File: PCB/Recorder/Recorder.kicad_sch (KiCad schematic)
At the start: 47 parts, among them J1 Battery, J2 Reset, J3 TC2030-USB-NL-DS, J4 TF_PUSH, J5 USB-C-Socket-H, Q2 CJ2301, SW1 SW_Push, U1 R, U2 L, U3 TP4054, U4 ME6211C33M5G-N, U6 ESP32-S3-MINI-1

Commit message: Started new Intercom
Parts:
- U6: value ESP32-S3-MINI-1 -> ESP32-S3-MINI-1-N4R2
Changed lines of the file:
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@@
 			)
 		)
-		(property "Value" "ESP32-S3-MINI-1"
+		(property "Value" "ESP32-S3-MINI-1-N4R2"
 			(at 50.8 45.5696 0)
 			(effects

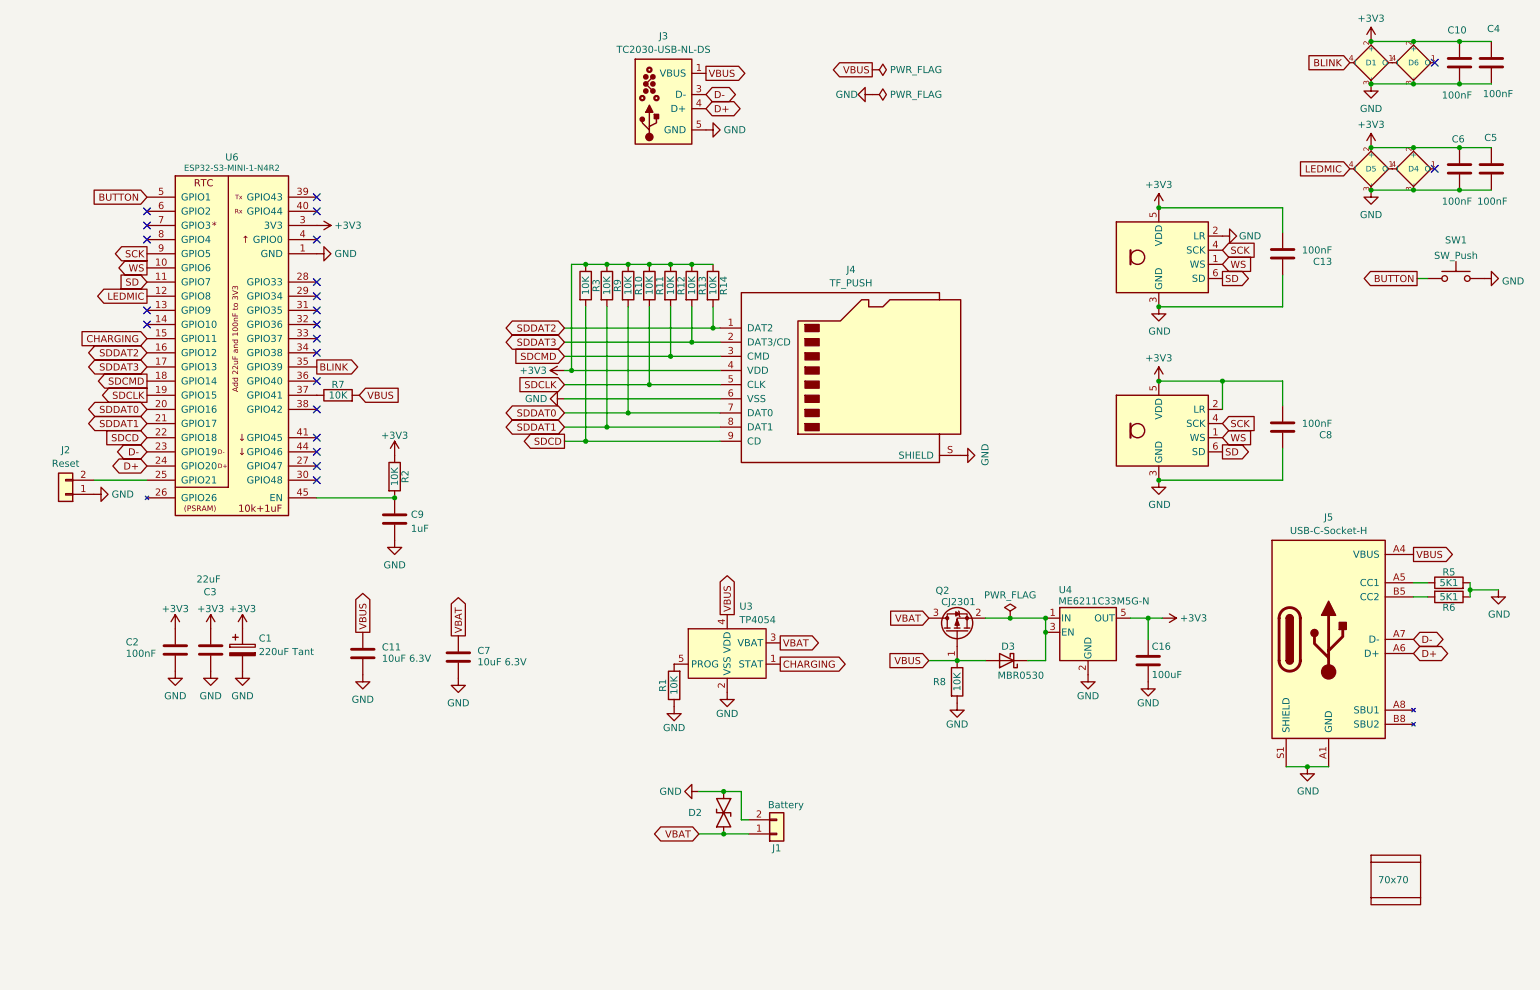
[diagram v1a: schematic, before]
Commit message: Power control for LEDs
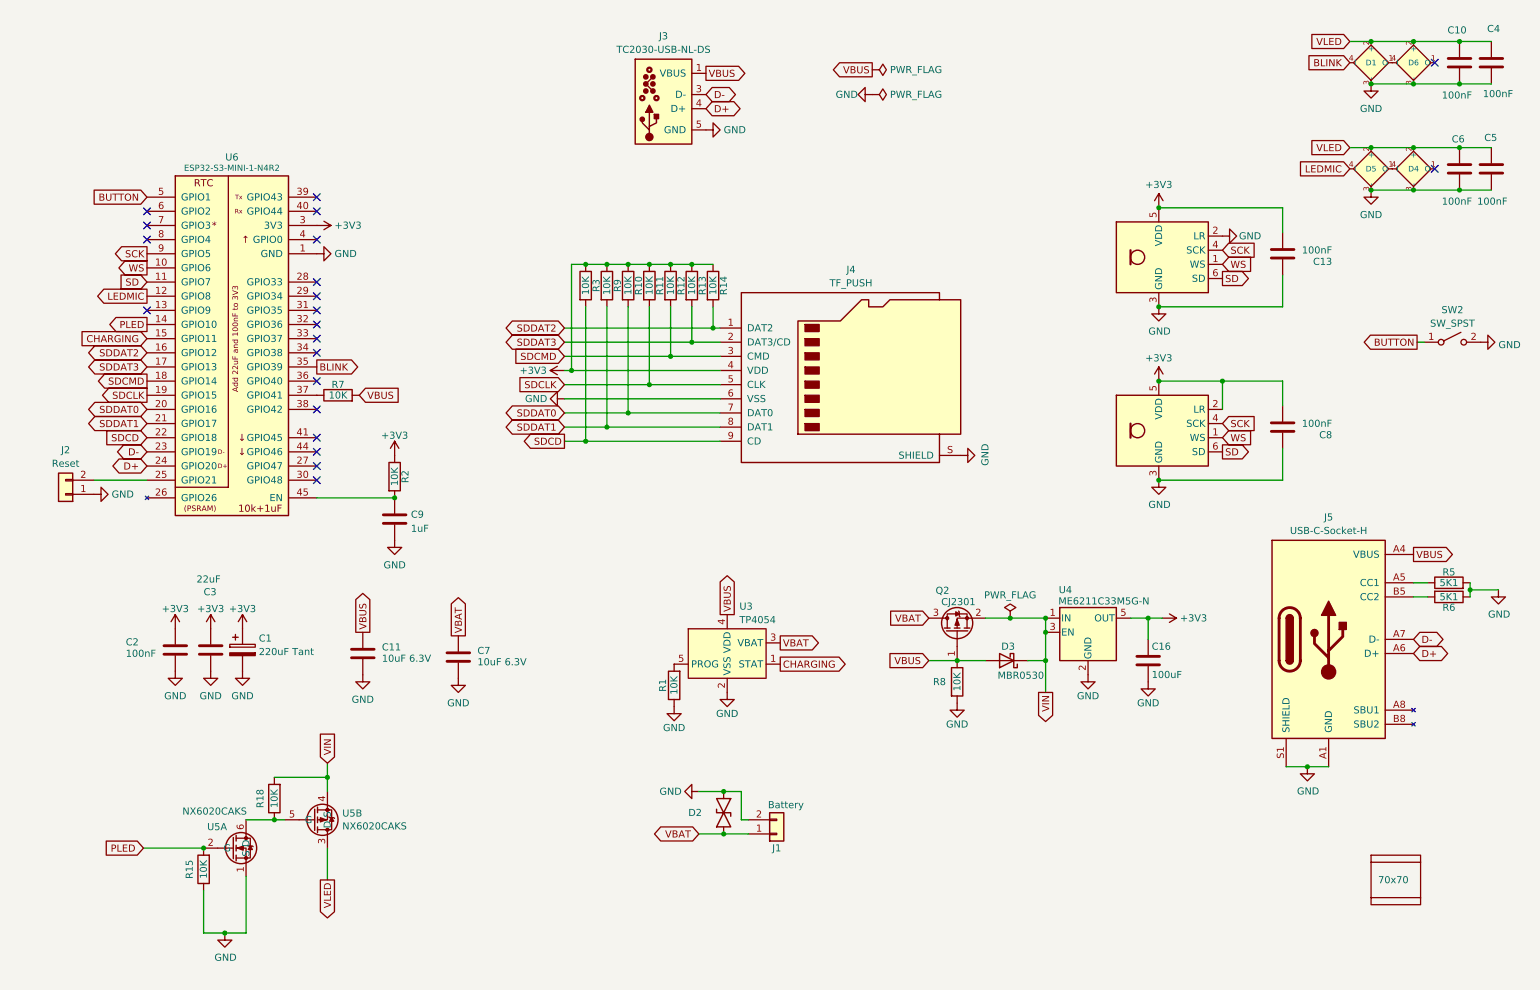
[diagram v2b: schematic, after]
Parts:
- removed SW1: SW_Push, RevK:TS-1092S-B3D2-G, symbol Switch:SW_Push
- added R15, R18: 10K, RevK:R_0402, symbol Device:R
- added SW2: SW_SPST, Button_Switch_SMD:SW_Push_1TS009xxxx-xxxx-xxxx_6x6x5mm, symbol Switch:SW_SPST
- added U5: NX6020CAKS, RevK:SOT-363_SC-70-6, symbol RevK:NX6020CAKS
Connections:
- net +3V3: no longer C10.1, C4.1, C5.1, C6.1, D1.2 (+), D4.2 (+), D5.2 (+), D6.2 (+)
- net BUTTON: now also SW2.1 (A)
- net GND: now also R15.1, SW2.2 (B), U5.1 (S)
- net VIN: now reaches D3.1 (K), Q2.2 (S), U4.1 (IN), U4.3 (EN)
- net VIN: now also R18.2, U5.4 (S)
- net PLED: now reaches U6.14 (GPIO10)
- net PLED: now also R15.2, U5.2 (G)
- new net: R18.1, U5.5 (G), U5.6 (D)
- new net VLED: C10.1, C4.1, C5.1, C6.1, D1.2 (+), D4.2 (+), D5.2 (+), D6.2 (+), U5.3 (D)
- no-connect marks 22 -> 21

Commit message: Clean up
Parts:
- U4: footprint RevK:SOT-23-5 -> RevK:SOT-23-5-90
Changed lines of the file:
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@@
 			)
 		)
-		(property "Footprint" "RevK:SOT-23-5"
+		(property "Footprint" "RevK:SOT-23-5-90"
 			(at 204.47 120.65 0)
 			(effects

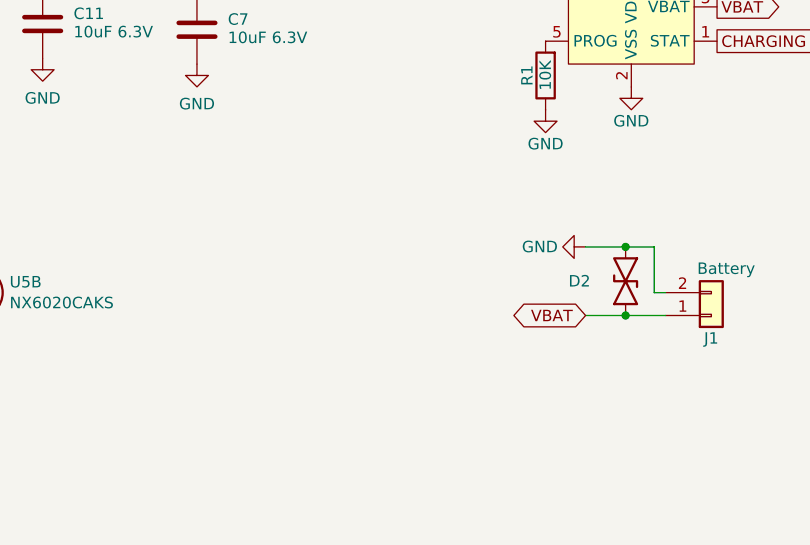
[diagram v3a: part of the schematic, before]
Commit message: New battery case
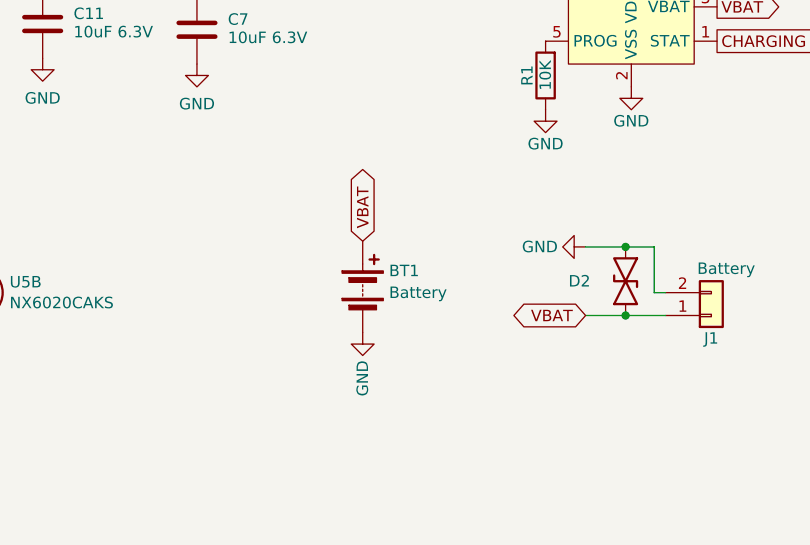
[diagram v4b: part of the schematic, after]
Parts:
- added BT1: Battery, RevK:LiPo1, symbol Device:Battery
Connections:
- net GND: now also BT1.2 (-)
- net VBAT: now also BT1.1 (+)
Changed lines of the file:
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@@
+		)
+	)
+	(global_label "VBAT"
+		(shape bidirectional)
+		(at 109.855 156.845 90)
+		(fields_autoplaced yes)
+		(effects
+			(font
+				(size 1.27 1.27)
+			)
+			(justify left)
+		)
+		(property "Intersheetrefs" "${INTERSHEET_REFS}"
+			(at 109.855 149.1467 90)
+			(effects
+				(font
+					(size 1.27 1.27)
+				)
+				(justify left)
+				(hide yes)
+			)
 		)
 	)
@@
 	)
 	(symbol
+		(lib_id "power:GND")
+		(at 109.855 167.005 0)
+		(unit 1)
+		(exclude_from_sim no)
+		(in_bom yes)
+		(on_board yes)
+		(dnp no)
+		(property "Reference" "#PWR030"
+			(at 109.855 173.355 0)
+			(effects
+				(font
+					(size 1.27 1.27)
+				)
+				(hide yes)
+			)
+		)
+		(property "Value" "GND"
+			(at 109.855 172.085 90)
+			(effects
+				(font
+					(size 1.27 1.27)
+				)
+			)
+		)
+		(property "Footprint" ""
+			(at 109.855 167.005 0)
+			(effects
+				(font
+					(size 1.27 1.27)
+				)
+				(hide yes)
+			)
+		)
+		(property "Datasheet" ""
+			(at 109.855 167.005 0)
+			(effects
+				(font
+					(size 1.27 1.27)
+				)
+				(hide yes)
+			)
+		)
+		(property "Description" "Power symbol creates a global label with name \"GND\" , ground"
+			(at 109.855 167.005 0)
+			(effects
+				(font
+					(size 1.27 1.27)
+				)
+				(hide yes)
+			)
+		)
+		(pin "1"
+		)
+		(instances
+			(project "Recorder"
+				(path "/46c350bb-7de4-4e81-aafd-4af55e37aab0"
+					(reference "#PWR030")
+					(unit 1)
+				)
+			)
+		)
+	)
+	(symbol
 		(lib_id "Device:C")
 		(at 74.295 132.715 0)
@@
 					(unit 1)
 				)
+			)
+		)
+	)
+	(symbol
+		(lib_id "Device:Battery")
+		(at 109.855 161.925 0)
+		(unit 1)
+		(exclude_from_sim no)
+		(in_bom no)
+		(on_board yes)
+		(dnp no)
+		(fields_autoplaced yes)
+		(property "Reference" "BT1"
+			(at 112.776 160.1413 0)
+			(effects
+				(font
+					(size 1.27 1.27)
+				)
+				(justify left)
+			)
+		)
+		(property "Value" "Battery"
+			(at 112.776 162.5656 0)
+			(effects
+				(font
+					(size 1.27 1.27)
+				)
+				(justify left)
+			)
+		)
+		(property "Footprint" "RevK:LiPo1"
+			(at 109.855 160.401 90)
+			(effects
+				(font
+					(size 1.27 1.27)
+				)
+				(hide yes)
+			)
+		)
+		(property "Datasheet" "~"
+			(at 109.855 160.401 90)
+			(effects
+				(font
+					(size 1.27 1.27)
+				)
+				(hide yes)
+			)
+		)
+		(property "Description" "Multiple-cell battery"
+			(at 109.855 161.925 0)
+			(effects
+				(font
+					(size 1.27 1.27)
+				)
+				(hide yes)
+			)
+		)
+		(pin "1"
+		)
+		(pin "2"
+		)
+		(instances
+			(project ""
+				(path "/46c350bb-7de4-4e81-aafd-4af55e37aab0"
+					(reference "BT1")
+					(unit 1)
+				)

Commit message: Library update
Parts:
- removed C7: 10uF 6.3V, RevK:C_0402, symbol Device:C
- removed J1: Battery, RevK:1.25T-2PWT (Molex 532610271), symbol Connector_Generic:Conn_01x02
- removed R18: 10K, RevK:R_0402, symbol Device:R
- removed SW2: SW_SPST, Button_Switch_SMD:SW_Push_1TS009xxxx-xxxx-xxxx_6x6x5mm, symbol Switch:SW_SPST
- removed U5: NX6020CAKS, RevK:SOT-363_SC-70-6, symbol RevK:NX6020CAKS
- added C1, C3: 22uF, RevK:C_0603, symbol Device:C
- added D1: D, RevK:D_0402, symbol Device:D
- added D10, D6, D8: XL-1010RGBC-WS2812B, RevK:SMD1010, symbol RevK:WS2812B-1mm
- added J6: Battery, RevK:1.25T-2PWT (Molex 532610271), symbol Connector_Generic:Conn_01x02
- added R14, R16: 100K 1%, RevK:R_0201, symbol Device:R
- added SW1: SW_Push_DPDT, RevK:SW_Push_DPDT, symbol RevK:SW_Push_DPDT
- added TP1, TP2: TestPoint, RevK:PAD-2mm, symbol Connector:TestPoint
- added U2: TPS22916CNYFPR, RevK:WCSP-4-0.78x0.78, symbol RevK:TPS22916
- C10: renamed from C13; footprint RevK:C_0402 -> RevK:C_0201
- C11: renamed from C8; footprint RevK:C_0402 -> RevK:C_0201
- C12: renamed from C10; footprint RevK:C_0402 -> RevK:C_0201
- C13: renamed from C6; footprint RevK:C_0402 -> RevK:C_0201
- C14: renamed from C4; footprint RevK:C_0402 -> RevK:C_0201
- C15: renamed from C5; footprint RevK:C_0402 -> RevK:C_0201
- C2: renamed from C9; footprint RevK:C_0402 -> RevK:C_0201
- C4: renamed from C2; footprint RevK:C_0402 -> RevK:C_0201
- R1: renamed from R7; footprint RevK:R_0402 -> RevK:R_0201; MPN (none) -> C106225
- R10: renamed from R14; footprint RevK:R_0402 -> RevK:R_0201; MPN (none) -> C106225
- R11: renamed from R8; footprint RevK:R_0402 -> RevK:R_0201; MPN (none) -> C106225
- R12: renamed from R5; footprint RevK:R_0402 -> RevK:R_0201; MPN (none) -> C274341
- R13: renamed from R6; footprint RevK:R_0402 -> RevK:R_0201; MPN (none) -> C274341
- R15: value 10K -> 100K 1%; footprint RevK:R_0402 -> RevK:R_0201; MPN (none) -> C717003
- R2, R3: footprint RevK:R_0402 -> RevK:R_0201; MPN (none) -> C106225
- R4: renamed from R9; footprint RevK:R_0402 -> RevK:R_0201; MPN (none) -> C106225
- R5: renamed from R10; footprint RevK:R_0402 -> RevK:R_0201; MPN (none) -> C106225
- R6: renamed from R11; footprint RevK:R_0402 -> RevK:R_0201; MPN (none) -> C106225
- R7: renamed from R12; footprint RevK:R_0402 -> RevK:R_0201; MPN (none) -> C106225
- R8: renamed from R1; value 10K -> 5K1; footprint RevK:R_0402 -> RevK:R_0201; MPN (none) -> C274341
- R9: renamed from R13; footprint RevK:R_0402 -> RevK:R_0201; MPN (none) -> C106225
- U4: Rotation Offset (none) -> 90
- U5: renamed from U2; value L -> ICS-43434
- U6: renamed from U1; value R -> ICS-43434
- renumbered C3 to C5, C1 to C6, C11 to C7, C16 to C9, D1 to D4, D6 to D5, D5 to D7, D4 to D9, J2 to J1, Q2 to Q1, U6 to U1
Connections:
- net BUTTON is gone; now on net CHARGING: U1.5 (GPIO1)
- net VLED is gone; now on net +3V3: C12.1, C13.1, C14.1, C15.1, D4.2 (+), D5.2 (+), D7.2 (+), D9.2 (+)
- net +3V3: now also D10.2 (+), D6.2 (+), D8.2 (+)
- net BLINK: now also U1.8 (GPIO4); no longer U1.35 (GPIO39)
- net CHARGING: no longer U1.15 (GPIO11)
- net D+: now also TP2.1
- net D-: now also TP1.1
- net GND: now also C1.2, C3.2, D10.3 (-), D6.3 (-), D8.3 (-), J6.2 (Pin_2), R16.2, SW1.5 (B), U2.B1 (GND); no longer R15.1
- net LEDMIC: now also U1.13 (GPIO9); no longer U1.12 (GPIO8)
- net at D5.1 (O): now also D6.4 (I)
- net at R1.1: now also U1.12 (GPIO8); no longer U1.37 (GPIO41)
- net PWR: now reaches U1.6 (GPIO2)
- net PWR: now also D1.2 (A)
- net BTN: now reaches U1.7 (GPIO3)
- net BTN: now also SW1.4 (C)
- net PLED: no longer names the net of U1.14 (GPIO10)
- net PLED: no longer R15.2
- net VBAT renamed VBATCHG
- net VBATCHG: now also C1.1, J6.1 (Pin_1), SW1.3 (C), U2.A2 (VIN); no longer Q1.3 (D)
- net VIN: no longer names the net of D3.1 (K), Q1.2 (S), U4.1 (IN), U4.3 (EN)
- new net: D1.1 (K), SW1.2 (B), U2.B2 (ON)
- new net: D10.4 (I), D8.1 (O)
- new net: D6.1 (O), D8.4 (I)
- new net: R14.2, R15.1
- new net ADC: R15.2, R16.1, U1.15 (GPIO11)
- new net VSWITCHED: C3.1, Q1.3 (D), R14.1, U2.A1 (VOUT)
- no-connect marks 21 -> 23
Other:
- note added: "5k1 is approx 200mA charge"
- note added: "CHRG Normal: on Full: off Reverse: off No battery: Twinkle"
- note added: "L"
- note added: "R"
- moved on the sheet: BT1, C4, C5, C6, C7, D4, D5, J3, R1

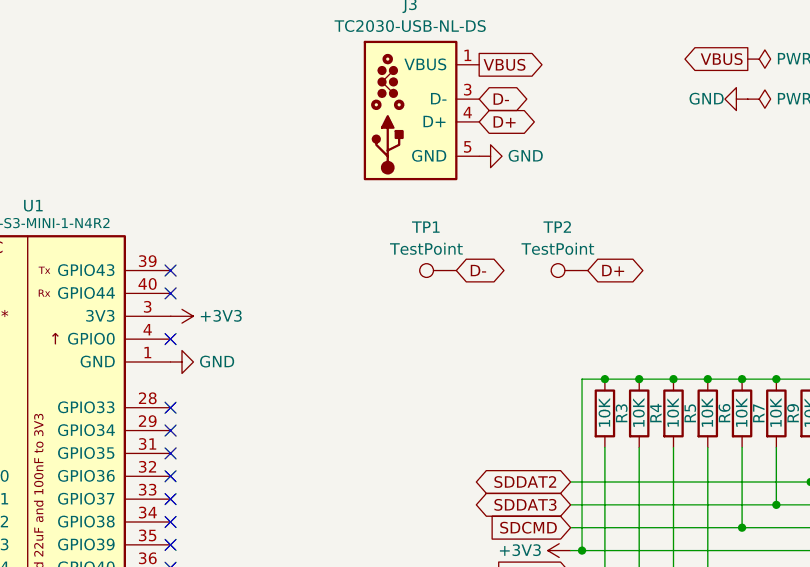
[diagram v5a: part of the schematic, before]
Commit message: v-cut
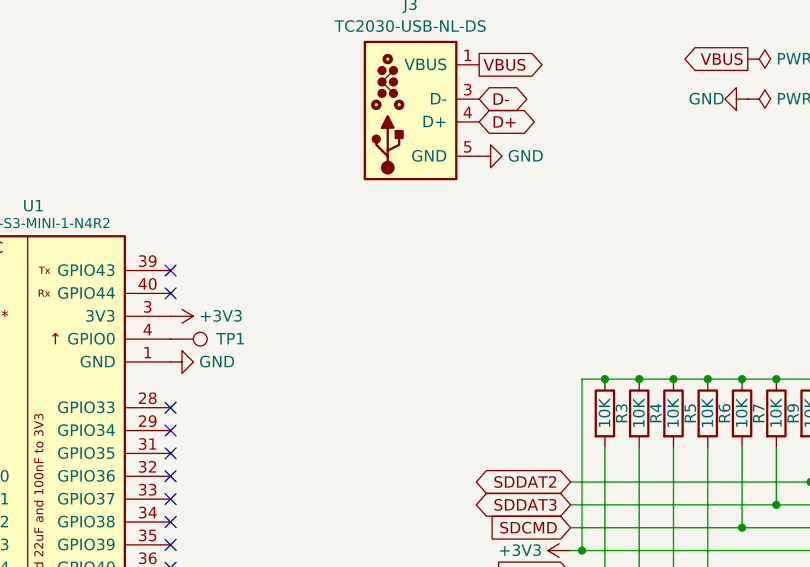
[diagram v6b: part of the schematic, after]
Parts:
- removed TP2: TestPoint, RevK:PAD-2mm, symbol Connector:TestPoint
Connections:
- net D-: no longer TP1.1
- net at U1.4 (GPIO0): now also TP1.1
- no-connect marks 23 -> 22
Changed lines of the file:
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@@
 	)
 	(no_connect
-		(at 66.04 58.42)
-	)
-	(no_connect
 		(at 34.925 155.575)
 	)
@@
 	(global_label "D+"
 		(shape bidirectional)
-		(at 112.395 50.8 0)
-		(fields_autoplaced yes)
-		(effects
-			(font
-				(size 1.27 1.27)
-			)
-			(justify left)
-		)
-		(property "Intersheetrefs" "${INTERSHEET_REFS}"
-			(at 118.5209 50.8 0)
-			(effects
-				(font
-					(size 1.27 1.27)
-				)
-				(justify left)
-				(hide yes)
-			)
-		)
-	)
-	(global_label "D+"
-		(shape bidirectional)
 		(at 100.33 34.29 0)
 		(fields_autoplaced yes)
@@
 		)
 	)
-	(global_label "D-"
-		(shape bidirectional)
-		(at 97.79 50.8 0)
-		(fields_autoplaced yes)
-		(effects
-			(font
-				(size 1.27 1.27)
-			)
-			(justify left)
-		)
-		(property "Intersheetrefs" "${INTERSHEET_REFS}"
-			(at 103.9159 50.8 0)
-			(effects
-				(font
-					(size 1.27 1.27)
-				)
-				(justify left)
-				(hide yes)
-			)
-		)
-	)
 	(global_label "PWR"
 		(shape output)
@@
 	)
 	(symbol
-		(lib_id "Connector:TestPoint")
-		(at 97.79 50.8 90)
-		(unit 1)
-		(exclude_from_sim no)
-		(in_bom yes)
-		(on_board yes)
-		(dnp no)
-		(fields_autoplaced yes)
-		(property "Reference" "TP1"
-			(at 94.488 46.0205 90)
-			(effects
-				(font
-					(size 1.27 1.27)
-				)
-			)
-		)
-		(property "Value" "TestPoint"
-			(at 94.488 48.4448 90)
-			(effects
-				(font
-					(size 1.27 1.27)
-				)
-			)
-		)
-		(property "Footprint" "RevK:PAD-2mm"
-			(at 97.79 45.72 0)
-			(effects
-				(font
-					(size 1.27 1.27)
-				)
-				(hide yes)
-			)
-		)
-		(property "Datasheet" "~"
-			(at 97.79 45.72 0)
-			(effects
-				(font
-					(size 1.27 1.27)
-				)
-				(hide yes)
-			)
-		)
-		(property "Description" "test point"
-			(at 97.79 50.8 0)
-			(effects
-				(font
-					(size 1.27 1.27)
-				)
-				(hide yes)
-			)
-		)
-		(pin "1"
-		)
-		(instances
-			(project ""
-				(path "/46c350bb-7de4-4e81-aafd-4af55e37aab0"
-					(reference "TP1")
-					(unit 1)
-				)
-			)
-		)
-	)
-	(symbol
 		(lib_id "power:GND")
 		(at 180.975 141.605 0)
@@
 	)
 	(symbol
-		(lib_id "Connector:TestPoint")
-		(at 112.395 50.8 90)
-		(unit 1)
-		(exclude_from_sim no)
-		(in_bom yes)
-		(on_board yes)
-		(dnp no)
-		(fields_autoplaced yes)
-		(property "Reference" "TP2"
-			(at 109.093 46.0205 90)
-			(effects
-				(font
-					(size 1.27 1.27)
-				)
-			)
-		)
-		(property "Value" "TestPoint"
-			(at 109.093 48.4448 90)
-			(effects
-				(font
-					(size 1.27 1.27)
-				)
-			)
-		)
-		(property "Footprint" "RevK:PAD-2mm"
-			(at 112.395 45.72 0)
-			(effects
-				(font
-					(size 1.27 1.27)
-				)
-				(hide yes)
-			)
-		)
-		(property "Datasheet" "~"
-			(at 112.395 45.72 0)
-			(effects
-				(font
-					(size 1.27 1.27)
-				)
-				(hide yes)
-			)
-		)
-		(property "Description" "test point"
-			(at 112.395 50.8 0)
-			(effects
-				(font
-					(size 1.27 1.27)
-				)
-				(hide yes)
-			)
-		)
-		(pin "1"
-		)
-		(instances
-			(project "Recorder"
-				(path "/46c350bb-7de4-4e81-aafd-4af55e37aab0"
-					(reference "TP2")
-					(unit 1)
-				)
-			)
-		)
-	)
-	(symbol
 		(lib_id "Device:R")
 		(at 130.175 138.43 180)
@@
 					(unit 1)
 				)
+			)
+		)
+	)
+	(symbol
+		(lib_id "Connector:TestPoint")
+		(at 66.04 58.42 270)
+		(unit 1)
+		(exclude_from_sim no)
+		(in_bom yes)
+		(on_board yes)
+		(dnp no)
+		(property "Reference" "TP1"
+			(at 71.12 58.42 90)
+			(effects
+				(font
+					(size 1.27 1.27)
+				)
+				(justify left)
+			)
+		)
+		(property "Value" "TestPoint"
+			(at 75.692 59.182 90)
+			(effects
+				(font
+					(size 1.27 1.27)
+				)
+				(justify left)
+				(hide yes)
+			)
+		)
+		(property "Footprint" "RevK:PAD-2mm"
+			(at 66.04 63.5 0)
+			(effects
+				(font
+					(size 1.27 1.27)
+				)
+				(hide yes)
+			)
+		)
+		(property "Datasheet" "~"
+			(at 66.04 63.5 0)
+			(effects
+				(font
+					(size 1.27 1.27)
+				)
+				(hide yes)
+			)
+		)
+		(property "Description" "test point"
+			(at 66.04 58.42 0)
+			(effects
+				(font
+					(size 1.27 1.27)
+				)
+				(hide yes)
+			)
+		)
+		(pin "1"
+		)
+		(instances
+			(project ""
+				(path "/46c350bb-7de4-4e81-aafd-4af55e37aab0"
+					(reference "TP1")
+					(unit 1)
+				)

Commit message: Render as order
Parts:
- TP1: now left out of the parts list
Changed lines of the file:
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@@
 		(unit 1)
 		(exclude_from_sim no)
-		(in_bom yes)
+		(in_bom no)
 		(on_board yes)
 		(dnp no)
